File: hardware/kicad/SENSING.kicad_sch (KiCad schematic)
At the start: 0 parts

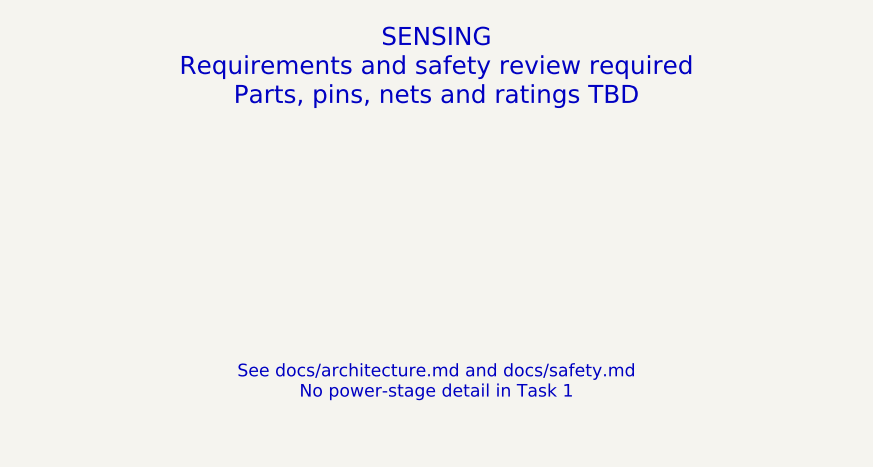
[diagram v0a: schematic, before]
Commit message: hardware: update existing KiCad architecture and add precharge sheet
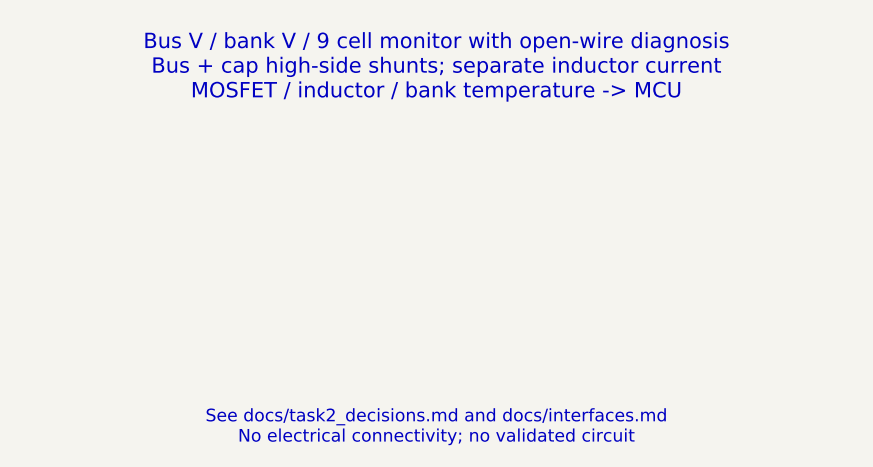
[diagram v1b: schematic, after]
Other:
- note added: "Bus V / bank V / 9 cell monitor with open-wire diagnosis Bus + cap high-side shunts; separate inductor current MOSFET / inductor / bank temperature -> MCU"
- note added: "See docs/task2_decisions.md and docs/interfaces.md No electrical connectivity; no validated circuit"
- note removed: "SENSING Requirements and safety review required Parts, pins, nets and ratings TBD"
- note removed: "See docs/architecture.md and docs/safety.md No power-stage detail in Task 1"
- title: SENSING - Placeholder -> SENSING - Task 2 Proposal

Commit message: hardware: implement prototype Rev A electrical schematic
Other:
- note added: "Electrical sensing now on CURRENT_SENSING, VOLTAGE_SENSING and TEMPERATURE_SENSING."
- note added: "Global labels connect actual package pins and wires across hierarchy. No firmware or PCB placement."
- note added: "Review all external assemblies, source-side tap protection and provisional ratings before energizing."
- note removed: "Bus V / bank V / 9 cell monitor with open-wire diagnosis Bus + cap high-side shunts; separate inductor current MOSFET / inductor / bank temperature -> MCU"
- note removed: "See docs/task2_decisions.md and docs/interfaces.md No electrical connectivity; no validated circuit"
- title: SENSING - Task 2 Proposal -> SENSING / Prototype Rev A draft
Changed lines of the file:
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@@
+(kicad_sch
+  (version 20250114)
+  (generator "eeschema")
+  (paper "User" 1189 841)
+  (title_block (title "SENSING / Prototype Rev A draft") (rev "RevA-draft") (comment 1 "ASSUMPTION - MUST VERIFY ON PROTOTYPE; no PCB placement"))
+  (text "Electrical sensing now on CURRENT_SENSING, VOLTAGE_SENSING and TEMPERATURE_SENSING."
+    (at 530 776 0)
+    (effects (font (size 1.3 1.3)))
+  )
+  (text "Global labels connect actual package pins and wires across hierarchy. No firmware or PCB placement."
+    (at 530 781 0)
+    (effects (font (size 1.3 1.3)))
+  )
+  (text "Review all external assemblies, source-side tap protection and provisional ratings before energizing."
+    (at 530 786 0)
+    (effects (font (size 1.3 1.3)))
+  )
+)
